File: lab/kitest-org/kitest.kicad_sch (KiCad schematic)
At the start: 3 parts, among them J1 Conn_01x02, J2 Conn_01x02, J3 Conn_01x04

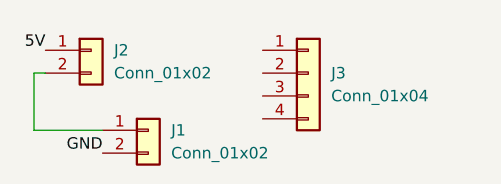
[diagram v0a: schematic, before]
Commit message: check if label is connected
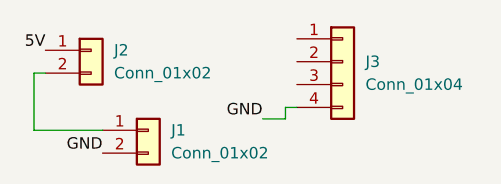
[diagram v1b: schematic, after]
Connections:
- net GND: now also J3.4 (Pin_4)
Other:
- moved on the sheet: J3
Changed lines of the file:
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@@
+	(wire
+		(pts
+			(xy 102.87 68.58) (xy 101.6 68.58)
+		)
+		(stroke
+			(width 0)
+			(type default)
+		)
+	)
+	(wire
+		(pts
+			(xy 101.6 69.85) (xy 99.06 69.85)
+		)
+		(stroke
+			(width 0)
+			(type default)
+		)
+	)
 	(wire
 		(pts
@@
 		)
 	)
+	(wire
+		(pts
+			(xy 101.6 68.58) (xy 101.6 69.85)
+		)
+		(stroke
+			(width 0)
+			(type default)
+		)
+	)
+	(label "GND"
+		(at 99.06 69.85 180)
+		(effects
+			(font
+				(size 1.27 1.27)
+			)
+			(justify right bottom)
+		)
+	)
 	(label "5V"
 		(at 74.93 62.23 180)
@@
 	(symbol
 		(lib_id "Connector_Generic:Conn_01x04")
-		(at 104.14 64.77 0)
+		(at 107.95 63.5 0)
 		(unit 1)
 		(exclude_from_sim no)
@@
 		(fields_autoplaced yes)
 		(property "Reference" "J3"
-			(at 106.68 64.7699 0)
+			(at 110.49 63.4999 0)
 			(effects
 				(font
@@
 		)
 		(property "Value" "Conn_01x04"
-			(at 106.68 67.3099 0)
+			(at 110.49 66.0399 0)
 			(effects
 				(font
@@
 		)
 		(property "Footprint" ""
-			(at 104.14 64.77 0)
+			(at 107.95 63.5 0)
 			(effects
 				(font
@@
 		)
 		(property "Datasheet" "~"
-			(at 104.14 64.77 0)
+			(at 107.95 63.5 0)
 			(effects
 				(font
@@
 		)
 		(property "Description" "Generic connector, single row, 01x04, script generated (kicad-library-utils/schlib/autogen/connector/)"
-			(at 104.14 64.77 0)
+			(at 107.95 63.5 0)
 			(effects
 				(font

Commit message: from scratch
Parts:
- J1: footprint (none) -> Connector_PinHeader_2.54mm:PinHeader_1x02_P2.54mm_Horizontal
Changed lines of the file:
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@@
 			)
 		)
-		(property "Footprint" ""
+		(property "Footprint" "Connector_PinHeader_2.54mm:PinHeader_1x02_P2.54mm_Horizontal"
 			(at 86.36 71.12 0)
 			(effects
